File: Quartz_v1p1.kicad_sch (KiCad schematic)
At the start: 2 parts, among them J1 5747847-6, J2 5747847-6

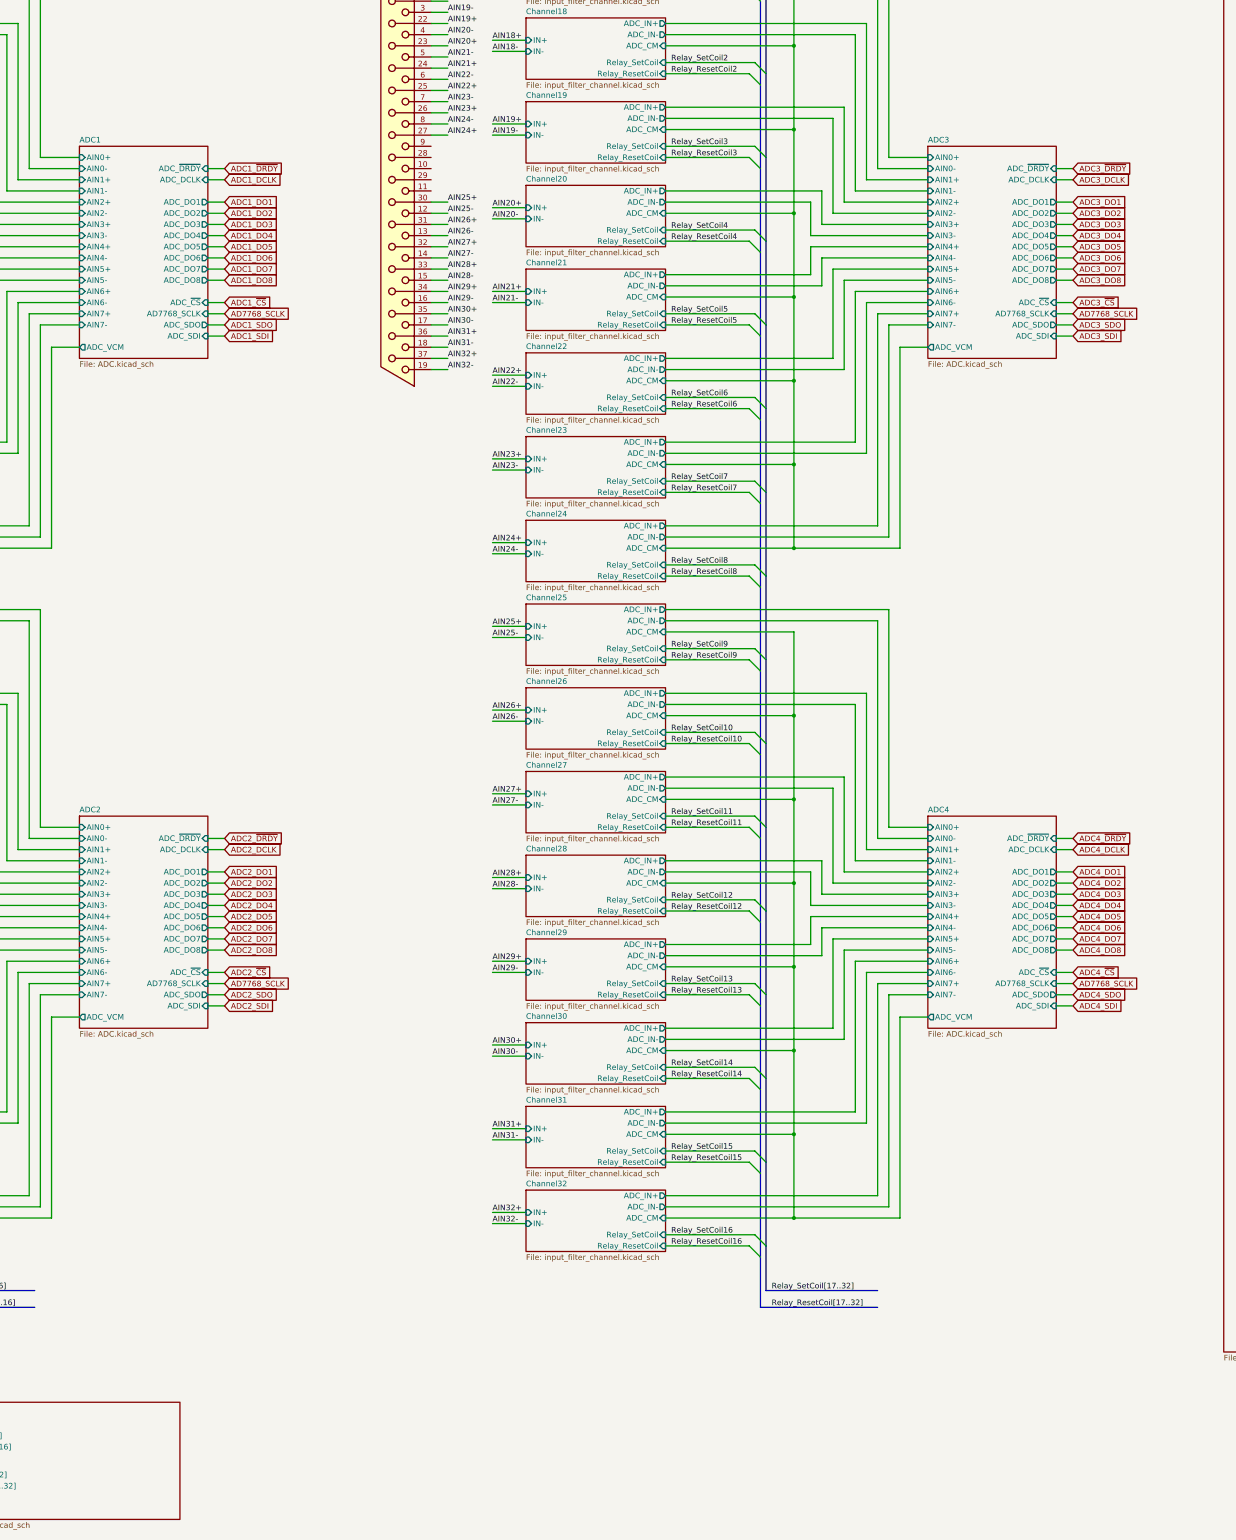
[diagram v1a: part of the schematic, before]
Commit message: Updated Schematics with recent changes
Made Updates with recent suggestions.
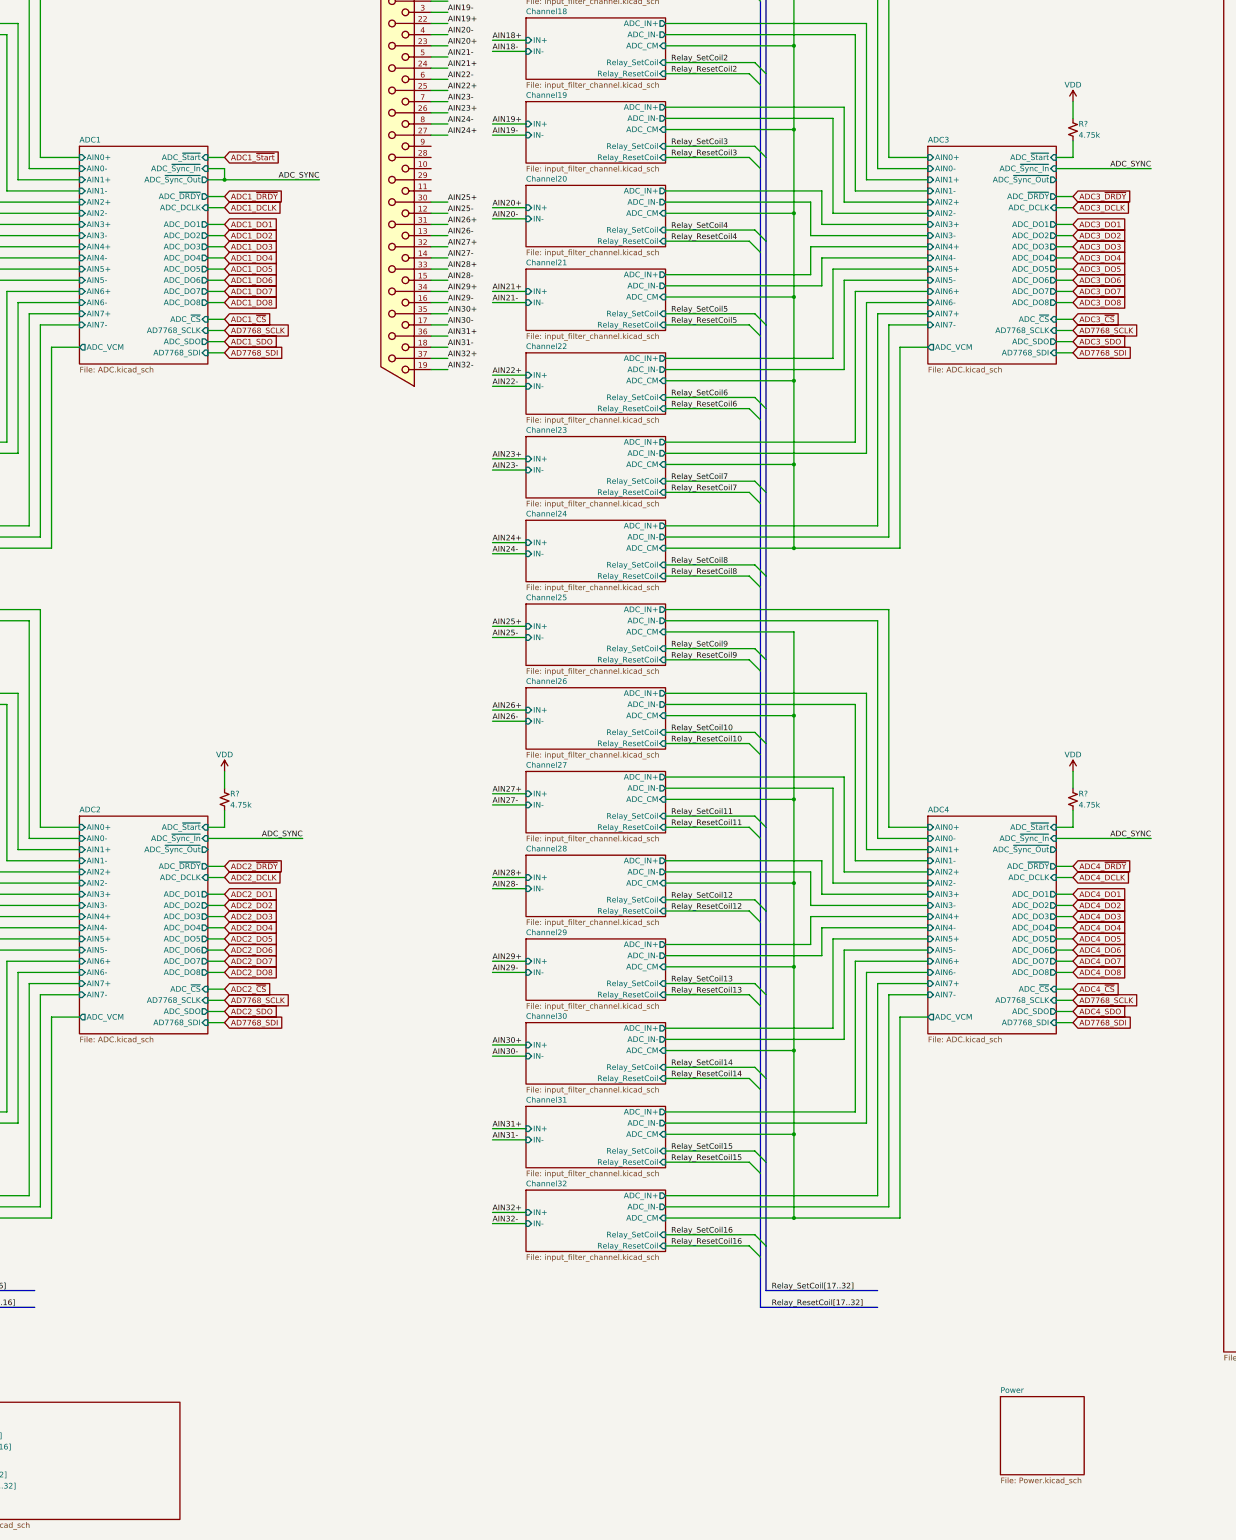
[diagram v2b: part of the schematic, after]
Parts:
- added R? (x3): 4.75k, symbol Device:R_Small_US
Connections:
- new net ADC2/ADC_~{Start}: R?.2
- new net ADC3/ADC_~{Start}: R?.2
- new net ADC4/ADC_~{Start}: R?.2
- new net VDD: R?.1, R?.1, R?.1
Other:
- added sheet Power (Power.kicad_sch)
- sheet ADC1 ports: added AD7768_SDI, ADC_~{Start}, ADC_~{Sync_In}, ADC_~{Sync_Out}; removed ADC_SDI
- sheet ADC2 ports: added AD7768_SDI, ADC_~{Start}, ADC_~{Sync_In}, ADC_~{Sync_Out}; removed ADC_SDI
- sheet ADC3 ports: added AD7768_SDI, ADC_~{Start}, ADC_~{Sync_In}, ADC_~{Sync_Out}; removed ADC_SDI
- sheet ADC4 ports: added AD7768_SDI, ADC_~{Start}, ADC_~{Sync_In}, ADC_~{Sync_Out}; removed ADC_SDI

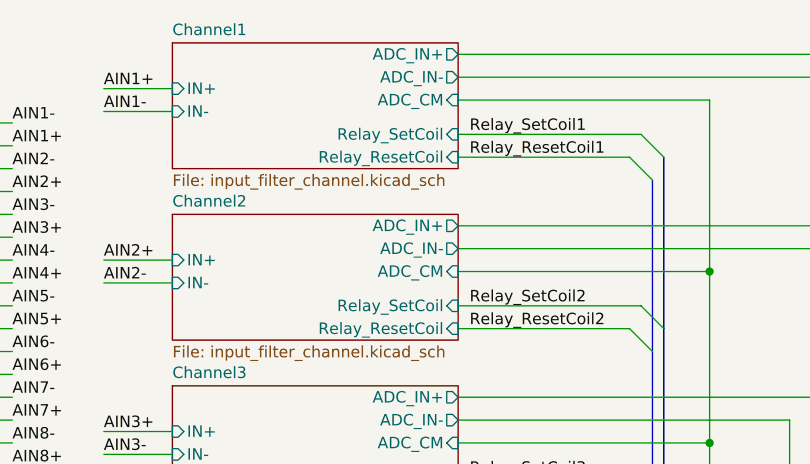
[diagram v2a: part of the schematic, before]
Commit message: Updated Channel 1 and fixes from review
Updated Channel 1 to use the INA851.
Fixed the ORNTA part pinout.
Fixed feedback on LT1763s.
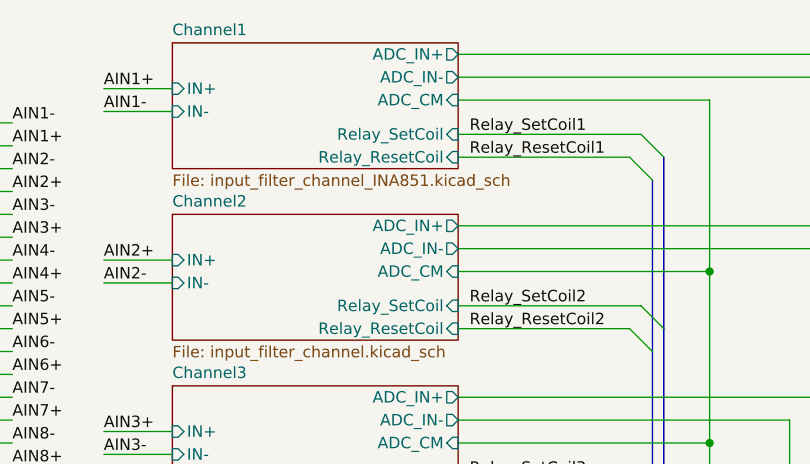
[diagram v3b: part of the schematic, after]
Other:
- sheet Channel1: file input_filter_channel.kicad_sch -> input_filter_channel_INA851.kicad_sch
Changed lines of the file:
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@@
       (effects (font (size 1.27 1.27)) (justify left bottom))
     )
-    (property "Sheetfile" "input_filter_channel.kicad_sch" (at 109.22 38.6846 0)
+    (property "Sheetfile" "input_filter_channel_INA851.kicad_sch" (at 109.22 38.6846 0)
       (effects (font (size 1.27 1.27)) (justify left top))
     )

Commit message: Schmatic Updates
Updated:
ADC MCLK signal
Removed PMOD connectors
Added Coax input for iRIG signal with 5V buffer
Moved around FMC pin mapping
Changed relay driver chip daisy chain order
Changed all input AFE to new design based around the INA851 chip
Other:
- sheet Channel10: file input_filter_channel.kicad_sch -> input_filter_channel_INA851.kicad_sch
- sheet Channel11: file input_filter_channel.kicad_sch -> input_filter_channel_INA851.kicad_sch
- sheet Channel12: file input_filter_channel.kicad_sch -> input_filter_channel_INA851.kicad_sch
- sheet Channel13: file input_filter_channel.kicad_sch -> input_filter_channel_INA851.kicad_sch
- sheet Channel14: file input_filter_channel.kicad_sch -> input_filter_channel_INA851.kicad_sch
- sheet Channel15: file input_filter_channel.kicad_sch -> input_filter_channel_INA851.kicad_sch
- sheet Channel16: file input_filter_channel.kicad_sch -> input_filter_channel_INA851.kicad_sch
- sheet Channel17: file input_filter_channel.kicad_sch -> input_filter_channel_INA851.kicad_sch
- sheet Channel18: file input_filter_channel.kicad_sch -> input_filter_channel_INA851.kicad_sch
- sheet Channel19: file input_filter_channel.kicad_sch -> input_filter_channel_INA851.kicad_sch
- sheet Channel2: file input_filter_channel.kicad_sch -> input_filter_channel_INA851.kicad_sch
- sheet Channel20: file input_filter_channel.kicad_sch -> input_filter_channel_INA851.kicad_sch
- sheet Channel21: file input_filter_channel.kicad_sch -> input_filter_channel_INA851.kicad_sch
- sheet Channel22: file input_filter_channel.kicad_sch -> input_filter_channel_INA851.kicad_sch
- sheet Channel23: file input_filter_channel.kicad_sch -> input_filter_channel_INA851.kicad_sch
- sheet Channel24: file input_filter_channel.kicad_sch -> input_filter_channel_INA851.kicad_sch
- sheet Channel25: file input_filter_channel.kicad_sch -> input_filter_channel_INA851.kicad_sch
- sheet Channel26: file input_filter_channel.kicad_sch -> input_filter_channel_INA851.kicad_sch
- sheet Channel27: file input_filter_channel.kicad_sch -> input_filter_channel_INA851.kicad_sch
- sheet Channel28: file input_filter_channel.kicad_sch -> input_filter_channel_INA851.kicad_sch
- sheet Channel29: file input_filter_channel.kicad_sch -> input_filter_channel_INA851.kicad_sch
- sheet Channel3: file input_filter_channel.kicad_sch -> input_filter_channel_INA851.kicad_sch
- sheet Channel30: file input_filter_channel.kicad_sch -> input_filter_channel_INA851.kicad_sch
- sheet Channel31: file input_filter_channel.kicad_sch -> input_filter_channel_INA851.kicad_sch
- sheet Channel32: file input_filter_channel.kicad_sch -> input_filter_channel_INA851.kicad_sch
- sheet Channel4: file input_filter_channel.kicad_sch -> input_filter_channel_INA851.kicad_sch
- sheet Channel5: file input_filter_channel.kicad_sch -> input_filter_channel_INA851.kicad_sch
- sheet Channel6: file input_filter_channel.kicad_sch -> input_filter_channel_INA851.kicad_sch
- sheet Channel7: file input_filter_channel.kicad_sch -> input_filter_channel_INA851.kicad_sch
- sheet Channel8: file input_filter_channel.kicad_sch -> input_filter_channel_INA851.kicad_sch
- sheet Channel9: file input_filter_channel.kicad_sch -> input_filter_channel_INA851.kicad_sch
